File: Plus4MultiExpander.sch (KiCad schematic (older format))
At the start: 17 parts, among them CN1 EDGE_CONN, CN2 C16_NEWSTYLE_EXP_PORT_1, CN3 C16_NEWSTYLE_EXP_PORT_2, CN4 C16_NEWSTYLE_EXP_PORT_3, U1 74HCT245, U2 74HCT245, U3 74HCT08

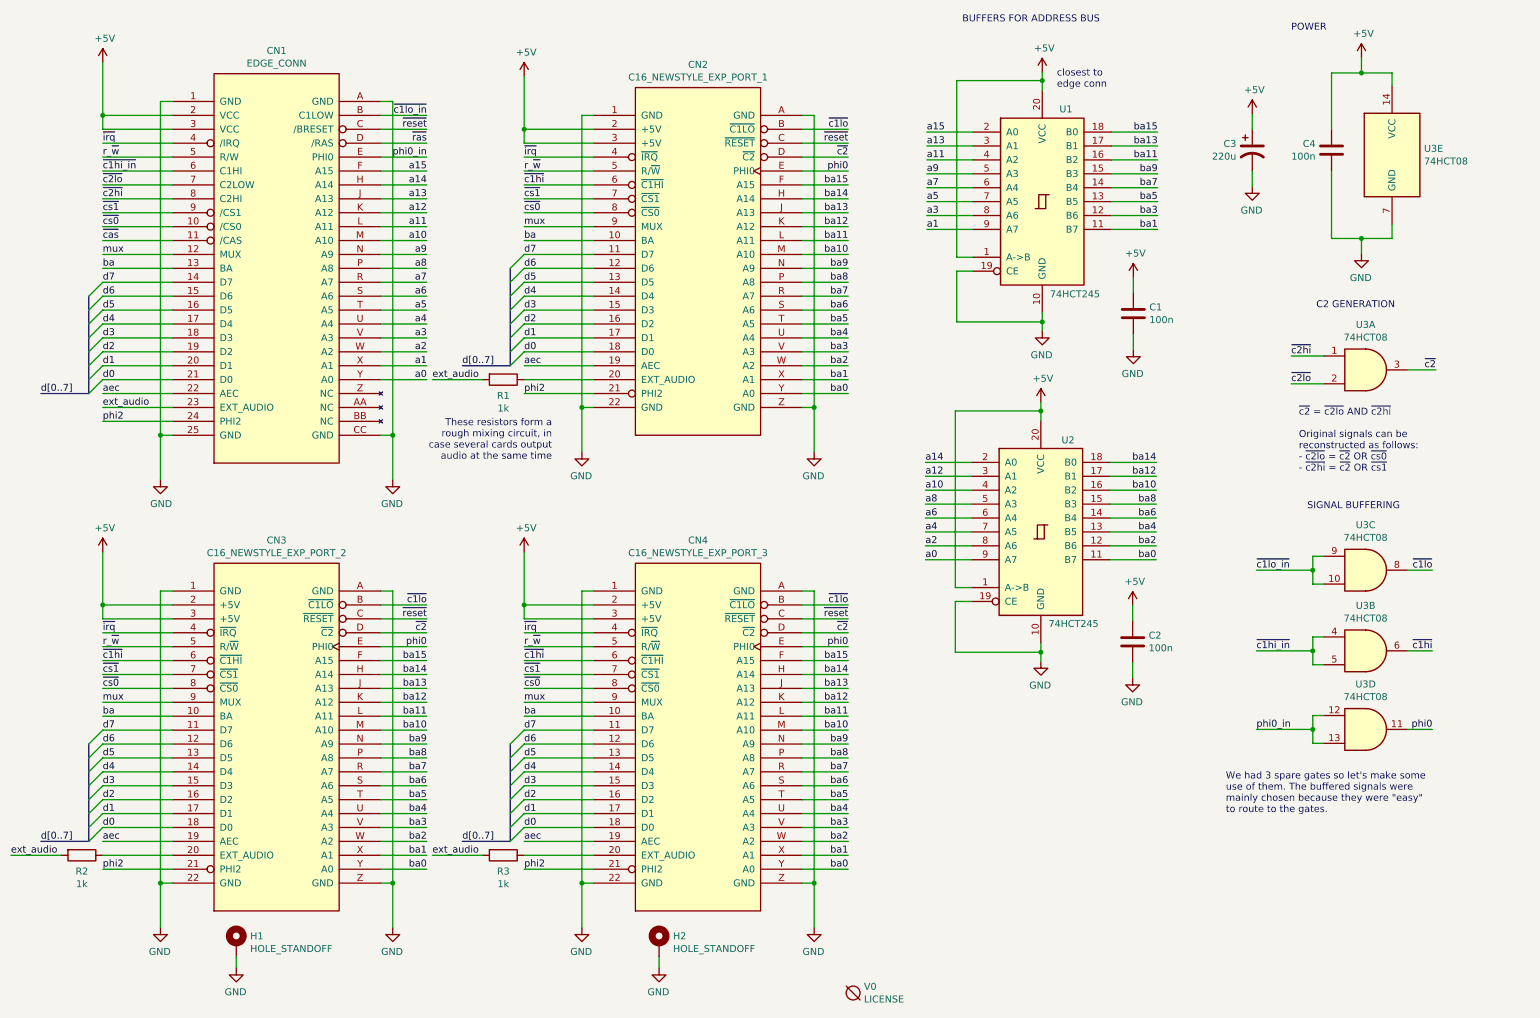
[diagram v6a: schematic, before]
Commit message: Buffer R/W instead of PHI0
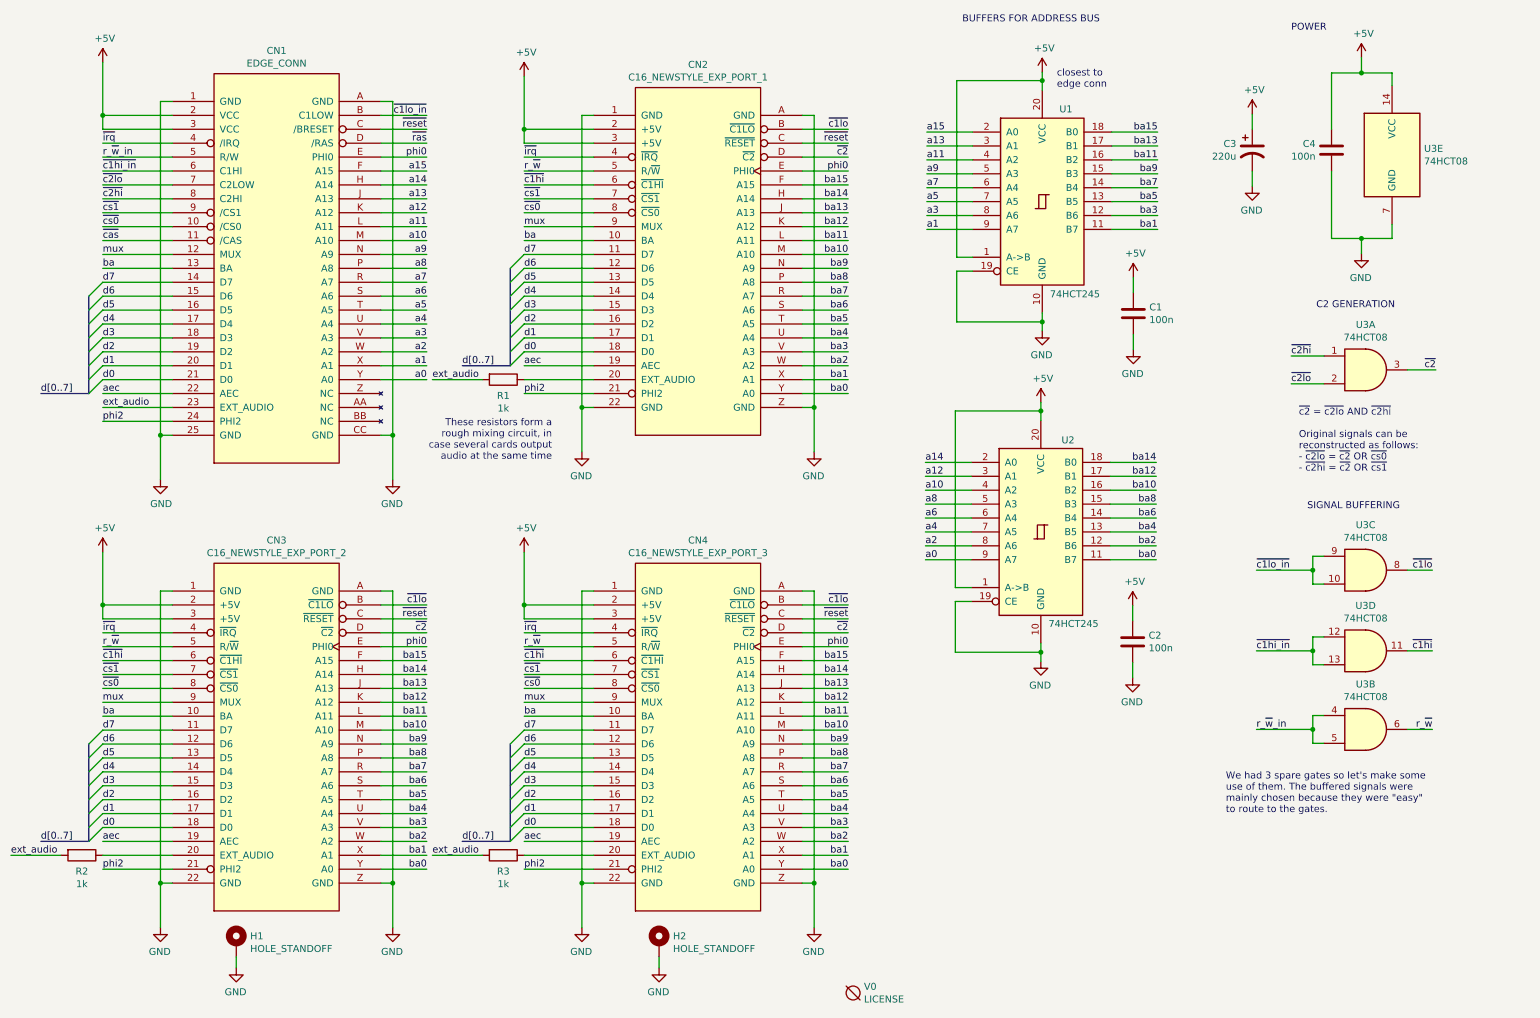
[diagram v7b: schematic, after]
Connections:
- net phi0: now also CN1.E (PHI0); no longer U3.11
- net r_~w: now also U3.6; no longer CN1.5 (R/W)
- net ~c1hi: now also U3.11; no longer U3.6
- net ~c1hi_in: now also U3.12, U3.13; no longer U3.4, U3.5
- removed net phi0_in: CN1.E (PHI0), U3.12, U3.13
- new net r_~w~_in: CN1.5 (R/W), U3.4, U3.5
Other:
- moved on the sheet: U3B, U3D
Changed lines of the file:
@@
 ~irq
 Text Label 1145 1645 0    50   ~ 0
-r_~w
+r_~w~_in
 Text Label 1145 1745 0    50   ~ 0
 ~c1hi_in
@@
 ~ras
 Text Label 3475 1645 2    50   ~ 0
-phi0_in
+phi0
 Wire Wire Line
 	3145 1845 3475 1845
@@
 L 74xx:74LS08 U3
 U 2 1 65AB918C
-P 10225 5195
-F 0 "U3" H 10225 5520 50  0000 C CNN
-F 1 "74HCT08" H 10225 5429 50  0000 C CNN
-F 2 "Package_DIP:DIP-14_W7.62mm_Socket_LongPads" H 10225 5195 50  0001 C CNN
-F 3 "http://www.ti.com/lit/gpn/sn74LS08" H 10225 5195 50  0001 C CNN
-	2    10225 5195
+P 10225 5760
+F 0 "U3" H 10225 6085 50  0000 C CNN
+F 1 "74HCT08" H 10225 5994 50  0000 C CNN
+F 2 "Package_DIP:DIP-14_W7.62mm_Socket_LongPads" H 10225 5760 50  0001 C CNN
+F 3 "http://www.ti.com/lit/gpn/sn74LS08" H 10225 5760 50  0001 C CNN
+	2    10225 5760
 	1    0    0    -1
 $EndComp
@@
 L 74xx:74LS08 U3
 U 4 1 65ABD51B
-P 10225 5760
-F 0 "U3" H 10225 6085 50  0000 C CNN
-F 1 "74HCT08" H 10225 5994 50  0000 C CNN
-F 2 "Package_DIP:DIP-14_W7.62mm_Socket_LongPads" H 10225 5760 50  0001 C CNN
-F 3 "http://www.ti.com/lit/gpn/sn74LS08" H 10225 5760 50  0001 C CNN
-	4    10225 5760
+P 10225 5195
+F 0 "U3" H 10225 5520 50  0000 C CNN
+F 1 "74HCT08" H 10225 5429 50  0000 C CNN
+F 2 "Package_DIP:DIP-14_W7.62mm_Socket_LongPads" H 10225 5195 50  0001 C CNN
+F 3 "http://www.ti.com/lit/gpn/sn74LS08" H 10225 5195 50  0001 C CNN
+	4    10225 5195
 	1    0    0    -1
 $EndComp
@@
 ~c1lo
 Text Label 9440 5760 0    50   ~ 0
-phi0_in
+r_~w~_in
 Wire Wire Line
 	9925 5660 9845 5660
@@
 	10525 5760 10705 5760
 Text Label 10705 5760 2    50   ~ 0
-phi0
+r_~w
 Text Notes 9805 4185 0    50   ~ 0
 SIGNAL BUFFERING

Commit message: Better routing
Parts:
- C3: footprint Capacitor_THT:CP_Radial_D8.0mm_P3.50mm -> Plus4MultiExpander:CP_Radial_L11.5mm_D8.0mm_P3.5mm_Horizontal
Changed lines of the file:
@@
 F 0 "C3" H 9295 1641 50  0000 R CNN
 F 1 "220u" H 9295 1550 50  0000 R CNN
-F 2 "Capacitor_THT:CP_Radial_D8.0mm_P3.50mm" H 9410 1595 50  0001 C CNN
+F 2 "Plus4MultiExpander:CP_Radial_L11.5mm_D8.0mm_P3.5mm_Horizontal" H 9410 1595 50  0001 C CNN
 F 3 "~" H 9410 1595 50  0001 C CNN
 	1    9410 1595
